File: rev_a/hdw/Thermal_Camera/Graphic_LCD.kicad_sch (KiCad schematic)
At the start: 14 parts, among them J2101 LCD Pixel Data, J2102 LCD CTP Data

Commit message: assigned some part numbers
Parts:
- C? (x2): Digi-Key PN (none) -> 490-10697-1-ND
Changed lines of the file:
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@@
 			)
 		)
-		(property "Digi-Key PN" ""
+		(property "Digi-Key PN" "490-10697-1-ND"
 			(at 117.856 281.432 0)
 			(effects
@@
 			)
 		)
-		(property "Digi-Key PN" ""
+		(property "Digi-Key PN" "490-10697-1-ND"
 			(at 67.056 280.162 0)
 			(effects

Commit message: assigned resistor part numbers
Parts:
- R? (x2): Digi-Key PN (none) -> RMCF0402FT10K0CT-ND
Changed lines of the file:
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@@
 			)
 		)
-		(property "Digi-Key PN" ""
+		(property "Digi-Key PN" "RMCF0402FT10K0CT-ND"
 			(at 223.52 60.96 0)
 			(effects
@@
 			)
 		)
-		(property "Digi-Key PN" ""
+		(property "Digi-Key PN" "RMCF0402FT10K0CT-ND"
 			(at 218.44 60.96 0)
 			(effects

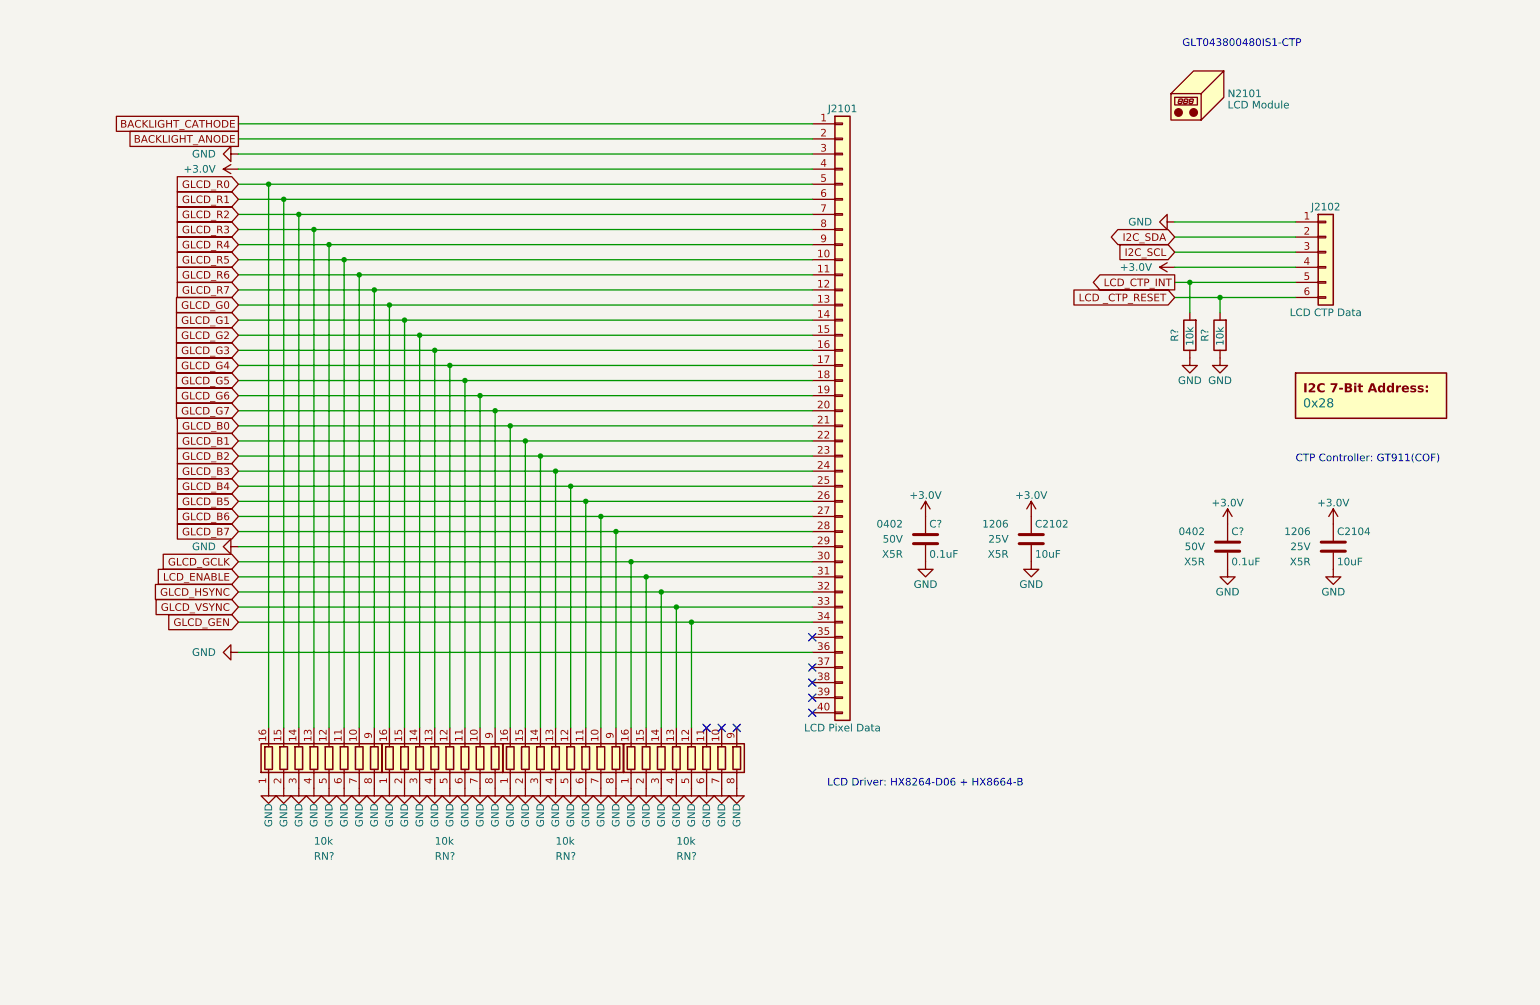
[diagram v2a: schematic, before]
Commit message: fixed LCD ribbon cable pinout, added footprint
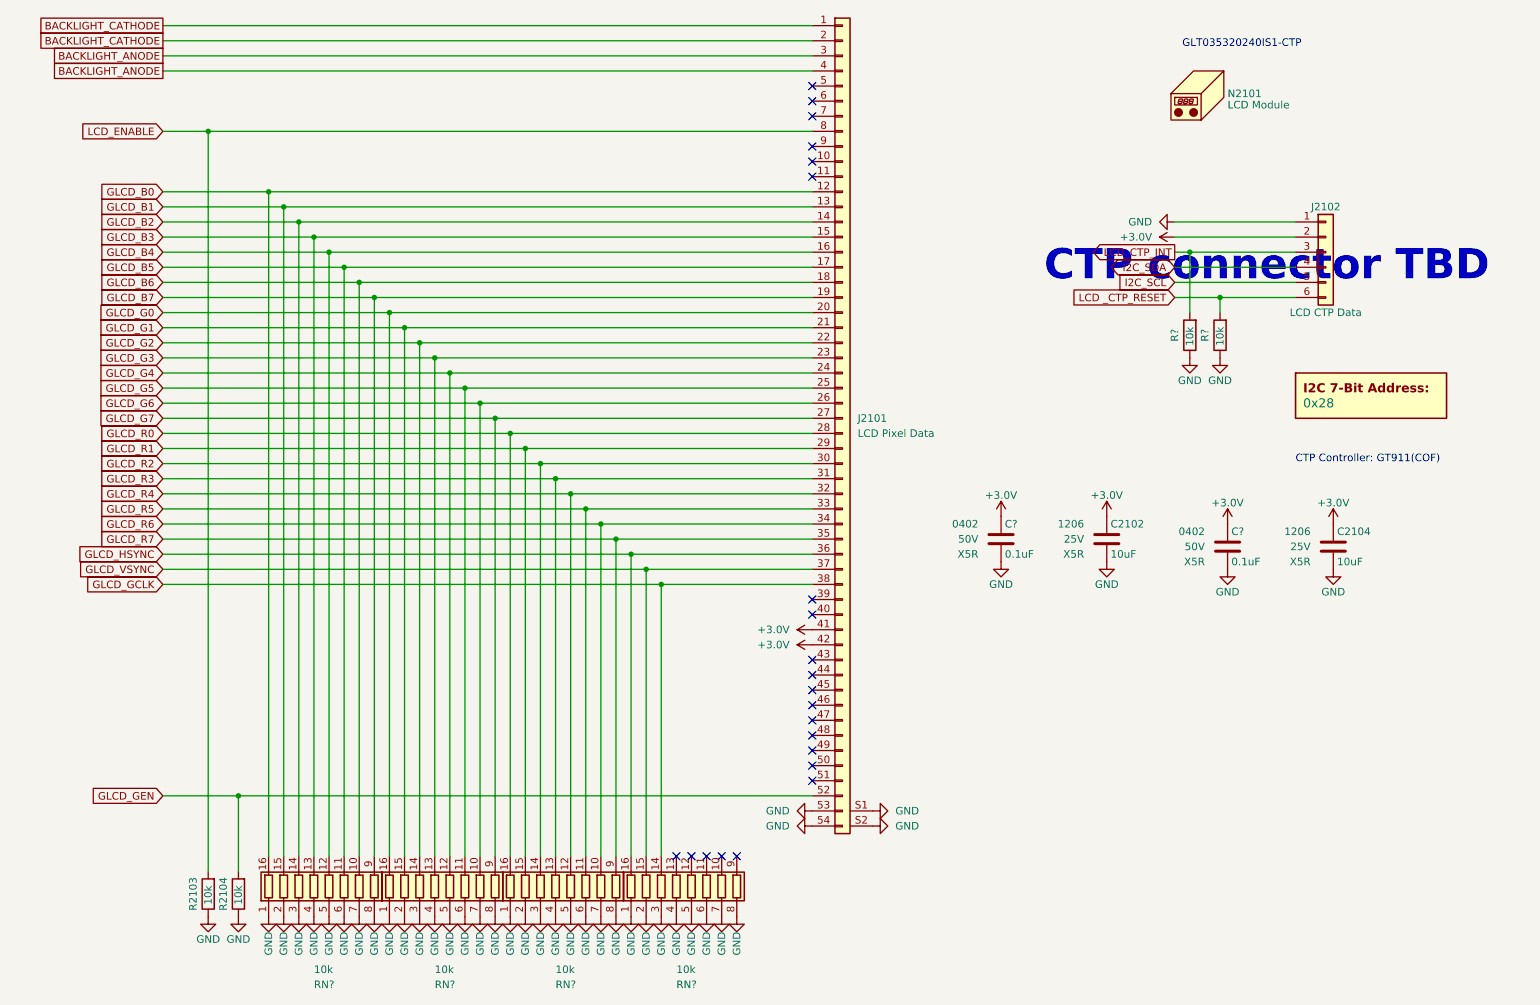
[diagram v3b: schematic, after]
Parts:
- added R2103, R2104: 10k, Resistors_SMD:R_0402, symbol Custom_Library:R_Custom
- J2101: footprint (none) -> Custom Footprints Library:GCT_FFC2B35-54-G_REVA2; symbol Connector_Generic:Conn_01x40 -> Connector_Generic:Conn_01x54
- N2101: Digi-Key PN 3390-GLT043800480IS1-CTP-ND -> GLT035320240IS1-CTP
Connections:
- net +3.0V: now also J2101.41 (Pin_41), J2101.42 (Pin_42), J2102.2 (Pin_2); no longer J2101.4 (Pin_4), J2102.4 (Pin_4)
- net BACKLIGHT_ANODE: now also J2101.3 (Pin_3), J2101.4 (Pin_4); no longer J2101.2 (Pin_2)
- net BACKLIGHT_CATHODE: now also J2101.2 (Pin_2)
- net GLCD_B0: now also J2101.12 (Pin_12), RN?.16 (R1.2); no longer J2101.21 (Pin_21), RN?.16 (R1.2)
- net GLCD_B1: now also J2101.13 (Pin_13), RN?.15 (R2.2); no longer J2101.22 (Pin_22), RN?.15 (R2.2)
- net GLCD_B2: now also J2101.14 (Pin_14), RN?.14 (R3.2); no longer J2101.23 (Pin_23), RN?.14 (R3.2)
- net GLCD_B3: now also J2101.15 (Pin_15), RN?.13 (R4.2); no longer J2101.24 (Pin_24), RN?.13 (R4.2)
- net GLCD_B4: now also J2101.16 (Pin_16), RN?.12 (R5.2); no longer J2101.25 (Pin_25), RN?.12 (R5.2)
- net GLCD_B5: now also J2101.17 (Pin_17), RN?.11 (R6.2); no longer J2101.26 (Pin_26), RN?.11 (R6.2)
- net GLCD_B6: now also J2101.18 (Pin_18), RN?.10 (R7.2); no longer J2101.27 (Pin_27), RN?.10 (R7.2)
- net GLCD_B7: now also J2101.19 (Pin_19), RN?.9 (R8.2); no longer J2101.28 (Pin_28), RN?.9 (R8.2)
- net GLCD_G0: now also J2101.20 (Pin_20); no longer J2101.13 (Pin_13)
- net GLCD_G1: now also J2101.21 (Pin_21); no longer J2101.14 (Pin_14)
- net GLCD_G2: now also J2101.22 (Pin_22); no longer J2101.15 (Pin_15)
- net GLCD_G3: now also J2101.23 (Pin_23); no longer J2101.16 (Pin_16)
- net GLCD_G4: now also J2101.24 (Pin_24); no longer J2101.17 (Pin_17)
- net GLCD_G5: now also J2101.25 (Pin_25); no longer J2101.18 (Pin_18)
- net GLCD_G6: now also J2101.26 (Pin_26); no longer J2101.19 (Pin_19)
- net GLCD_G7: now also J2101.27 (Pin_27); no longer J2101.20 (Pin_20)
- net GLCD_GCLK: now also J2101.38 (Pin_38), RN?.14 (R3.2); no longer J2101.30 (Pin_30), RN?.16 (R1.2)
- net GLCD_GEN: now also J2101.52 (Pin_52), R2104.1; no longer J2101.34 (Pin_34), RN?.12 (R5.2)
- net GLCD_HSYNC: now also J2101.36 (Pin_36), RN?.16 (R1.2); no longer J2101.32 (Pin_32), RN?.14 (R3.2)
- net GLCD_R0: now also J2101.28 (Pin_28), RN?.16 (R1.2); no longer J2101.5 (Pin_5), RN?.16 (R1.2)
- net GLCD_R1: now also J2101.29 (Pin_29), RN?.15 (R2.2); no longer J2101.6 (Pin_6), RN?.15 (R2.2)
- net GLCD_R2: now also J2101.30 (Pin_30), RN?.14 (R3.2); no longer J2101.7 (Pin_7), RN?.14 (R3.2)
- net GLCD_R3: now also J2101.31 (Pin_31), RN?.13 (R4.2); no longer J2101.8 (Pin_8), RN?.13 (R4.2)
- net GLCD_R4: now also J2101.32 (Pin_32), RN?.12 (R5.2); no longer J2101.9 (Pin_9), RN?.12 (R5.2)
- net GLCD_R5: now also J2101.33 (Pin_33), RN?.11 (R6.2); no longer J2101.10 (Pin_10), RN?.11 (R6.2)
- net GLCD_R6: now also J2101.34 (Pin_34), RN?.10 (R7.2); no longer J2101.11 (Pin_11), RN?.10 (R7.2)
- net GLCD_R7: now also J2101.35 (Pin_35), RN?.9 (R8.2); no longer J2101.12 (Pin_12), RN?.9 (R8.2)
- net GLCD_VSYNC: now also J2101.37 (Pin_37), RN?.15 (R2.2); no longer J2101.33 (Pin_33), RN?.13 (R4.2)
- net GND: now also J2101.53 (Pin_53), J2101.54 (Pin_54), J2101.S1, J2101.S2, R2103.2, R2104.2; no longer J2101.29 (Pin_29), J2101.3 (Pin_3), J2101.36 (Pin_36)
- net I2C_SCL: now also J2102.5 (Pin_5); no longer J2102.3 (Pin_3)
- net I2C_SDA: now also J2102.4 (Pin_4); no longer J2102.2 (Pin_2)
- net LCD_CTP_INT: now also J2102.3 (Pin_3); no longer J2102.5 (Pin_5)
- net LCD_ENABLE: now also J2101.8 (Pin_8), R2103.1; no longer J2101.31 (Pin_31), RN?.15 (R2.2)
- no-connect marks 8 -> 22
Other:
- note added: "CTP connector TBD"
- note added: "GLT035320240IS1-CTP"
- note removed: "GLT043800480IS1-CTP"
- note removed: "LCD Driver: HX8264-D06 + HX8664-B"
- moved on the sheet: C2102, C?, RN?

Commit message: generated rough LCD outline, made board outline
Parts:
- N2101: footprint (none) -> Custom Footprints Library:GLT035320240IS1-CTP
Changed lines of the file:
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@@
 			)
 		)
-		(property "Footprint" ""
+		(property "Footprint" "Custom Footprints Library:GLT035320240IS1-CTP"
 			(at 214.63 29.21 0)
 			(effects

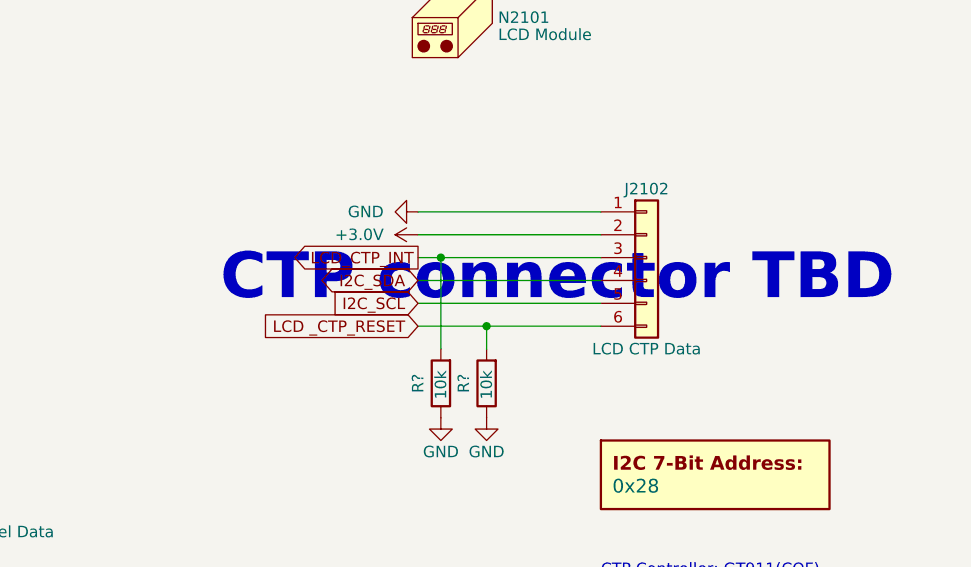
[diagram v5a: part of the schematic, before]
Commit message: assigned CTP connector footprint
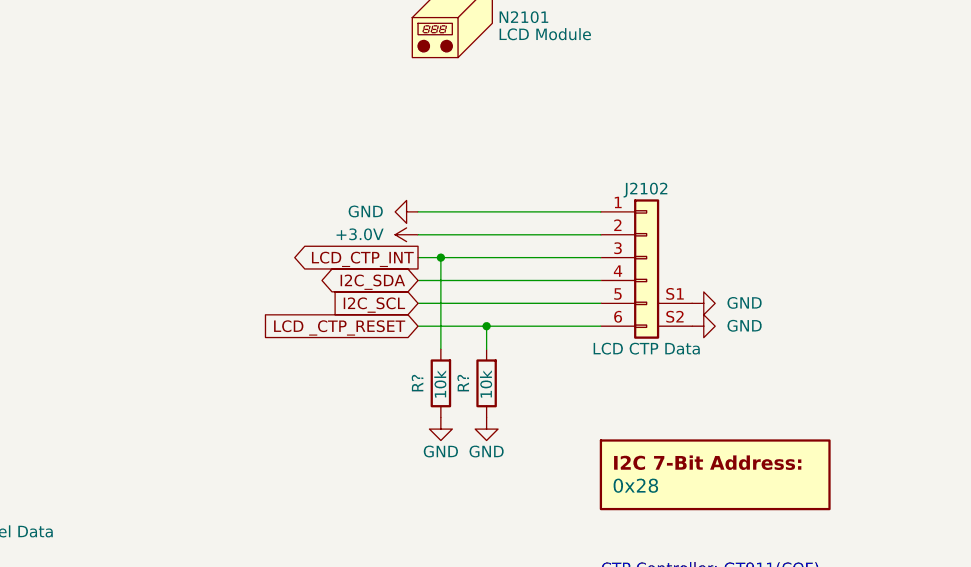
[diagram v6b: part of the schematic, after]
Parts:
- J2101: Digi-Key PN 26-FH12-40S-0.5SH(55)CT-ND -> 2073-FFC2B35-54-GCT-ND
- J2102: footprint (none) -> Custom Footprints Library:GCT_FFC2B35-06-G_REVA2; Digi-Key PN (none) -> 2073-FFC2B35-06-GCT-ND
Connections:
- net GND: now also J2102.S1, J2102.S2
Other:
- note removed: "CTP connector TBD"
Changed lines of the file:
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@@
 		)
 	)
-	(text "CTP connector TBD"
-		(exclude_from_sim no)
-		(at 223.774 59.436 0)
-		(effects
-			(font
-				(size 5.08 5.08)
-				(thickness 1.016)
-				(bold yes)
-				(color 255 0 0 1)
-			)
-		)
-	)
 	(text "GLT035320240IS1-CTP"
 		(exclude_from_sim no)
@@
 	(symbol
 		(lib_id "power:GND")
+		(at 238.76 62.23 90)
+		(mirror x)
+		(unit 1)
+		(exclude_from_sim no)
+		(in_bom yes)
+		(on_board yes)
+		(dnp no)
+		(property "Reference" "#PWR01"
+			(at 245.11 62.23 0)
+			(effects
+				(font
+					(size 1.27 1.27)
+				)
+				(hide yes)
+			)
+		)
+		(property "Value" "GND"
+			(at 242.57 62.23 90)
+			(effects
+				(font
+					(size 1.27 1.27)
+				)
+				(justify right)
+			)
+		)
+		(property "Footprint" ""
+			(at 238.76 62.23 0)
+			(effects
+				(font
+					(size 1.27 1.27)
+				)
+				(hide yes)
+			)
+		)
+		(property "Datasheet" ""
+			(at 238.76 62.23 0)
+			(effects
+				(font
+					(size 1.27 1.27)
+				)
+				(hide yes)
+			)
+		)
+		(property "Description" ""
+			(at 238.76 62.23 0)
+			(effects
+				(font
+					(size 1.27 1.27)
+				)
+				(hide yes)
+			)
+		)
+		(pin "1"
+		)
+		(instances
+			(project "Thermal_Camera"
+				(path "/4bd21e0b-5408-4b93-866e-c82ac5b31fa9/c2d59ecd-441a-4d58-9156-a852d244de52"
+					(reference "#PWR01")
+					(unit 1)
+				)
+			)
+		)
+	)
+	(symbol
+		(lib_id "power:GND")
 		(at 157.48 153.67 90)
 		(mirror x)
@@
 			)
 		)
-		(property "Digi-Key PN" "26-FH12-40S-0.5SH(55)CT-ND"
+		(property "Digi-Key PN" "2073-FFC2B35-54-GCT-ND"
 			(at 152.4 85.09 0)
 			(effects
@@
 			)
 		)
-		(property "Footprint" ""
+		(property "Footprint" "Custom Footprints Library:GCT_FFC2B35-06-G_REVA2"
 			(at 233.68 57.15 0)
 			(effects
@@
 			)
 		)
+		(property "Digi-Key PN" "2073-FFC2B35-06-GCT-ND"
+			(at 233.68 57.15 0)
+			(effects
+				(font
+					(size 1.27 1.27)
+				)
+				(hide yes)
+			)
+		)
 		(pin "1"
 		)
@@
 		(pin "6"
 		)
+		(pin "S2"
+		)
+		(pin "S1"
+		)
 		(instances
 			(project "Thermal_Camera"
@@
 					(unit 1)
 				)
+			)
+		)
+	)
+	(symbol
+		(lib_id "power:GND")
+		(at 238.76 64.77 90)
+		(mirror x)
+		(unit 1)
+		(exclude_from_sim no)
+		(in_bom yes)
+		(on_board yes)
+		(dnp no)
+		(property "Reference" "#PWR02"
+			(at 245.11 64.77 0)
+			(effects
+				(font
+					(size 1.27 1.27)
+				)
+				(hide yes)
+			)
+		)
+		(property "Value" "GND"
+			(at 242.57 64.77 90)
+			(effects
+				(font
+					(size 1.27 1.27)
+				)
+				(justify right)
+			)
+		)
+		(property "Footprint" ""
+			(at 238.76 64.77 0)
+			(effects
+				(font
+					(size 1.27 1.27)
+				)
+				(hide yes)
+			)
+		)
+		(property "Datasheet" ""
+			(at 238.76 64.77 0)
+			(effects
+				(font
+					(size 1.27 1.27)
+				)
+				(hide yes)
+			)
+		)
+		(property "Description" ""
+			(at 238.76 64.77 0)
+			(effects
+				(font
+					(size 1.27 1.27)
+				)
+				(hide yes)
+			)
+		)
+		(pin "1"
+		)
+		(instances
+			(project "Thermal_Camera"
+				(path "/4bd21e0b-5408-4b93-866e-c82ac5b31fa9/c2d59ecd-441a-4d58-9156-a852d244de52"
+					(reference "#PWR02")
+					(unit 1)
+				)
